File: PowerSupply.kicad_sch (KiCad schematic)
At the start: 13 parts

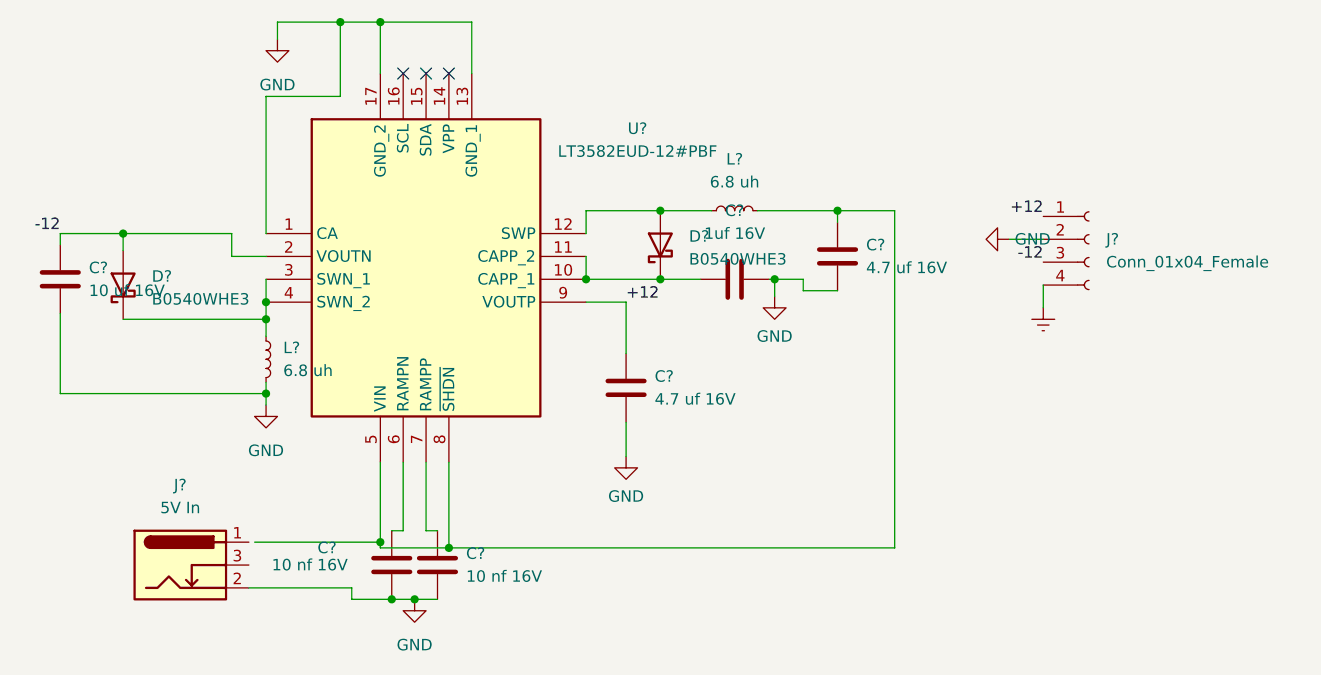
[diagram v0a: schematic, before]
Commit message: Board Basically done.  Just need to tweak the silkscreen.
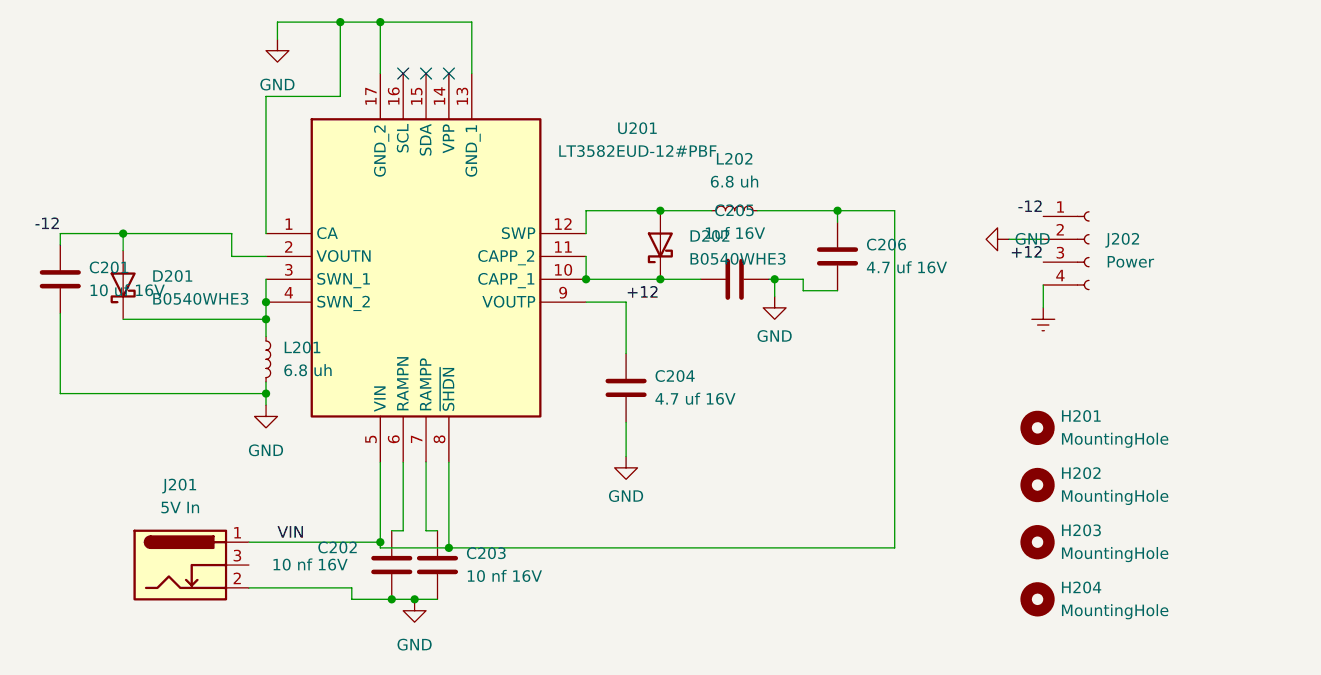
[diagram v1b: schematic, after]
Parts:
- added H201, H202, H203, H204: MountingHole, MountingHole:MountingHole_3.2mm_M3, symbol Mechanical:MountingHole
- J202: renamed from J?; value Conn_01x04_Female -> Power
- U201: renamed from U?; footprint (none) -> ExtraFootprints:QFN50P300X300X80-17N-D
- gave numbers to parts that had none: 11
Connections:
- net +12: now also J202.3 (Pin_3); no longer J202.1 (Pin_1)
- net -12: now also J202.1 (Pin_1); no longer J202.3 (Pin_3)
- net VIN: now reaches C206.1, L202.2, U201.5 (VIN), U201.8 (~{SHDN})
- net VIN: now also J201.1

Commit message: Footprint and 3D model updates.
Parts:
- J201: footprint Connector_BarrelJack:BarrelJack_Kycon_KLDX-0202-xC_Horizontal -> ExtraFootprints:KLDX0202AC
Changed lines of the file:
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@@
     (property "Reference" "J201" (id 0) (at 85.09 119.38 0))
     (property "Value" "5V In" (id 1) (at 85.09 121.92 0))
-    (property "Footprint" "Connector_BarrelJack:BarrelJack_Kycon_KLDX-0202-xC_Horizontal" (id 2) (at 86.36 129.286 0)
+    (property "Footprint" "ExtraFootprints:KLDX0202AC" (id 2) (at 86.36 129.286 0)
       (effects (font (size 1.27 1.27)) hide)
     )
